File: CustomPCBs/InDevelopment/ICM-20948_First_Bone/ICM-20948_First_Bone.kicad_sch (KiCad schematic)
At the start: 14 parts, among them J1 Conn_01x04_MountingPin, T1 BSS138BKS_115, U1 ICM-20948, U2 HE6206-18NR

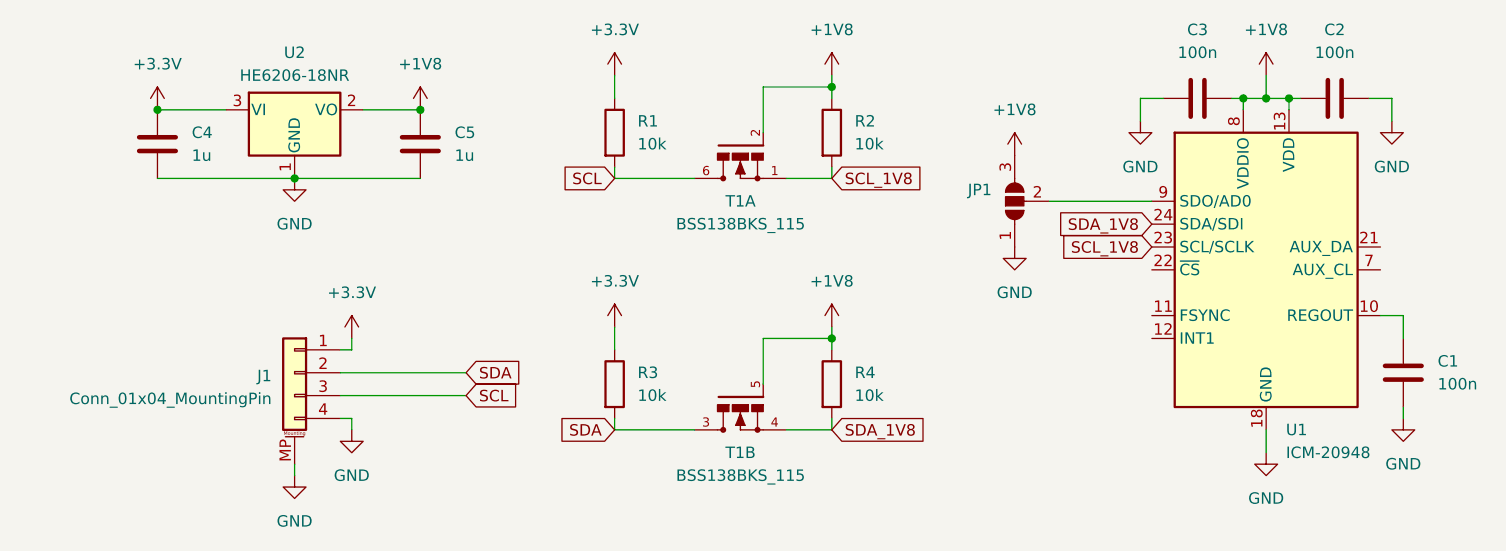
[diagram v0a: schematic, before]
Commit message: BMI160+mag board finished, fixed CS on ICM-20948
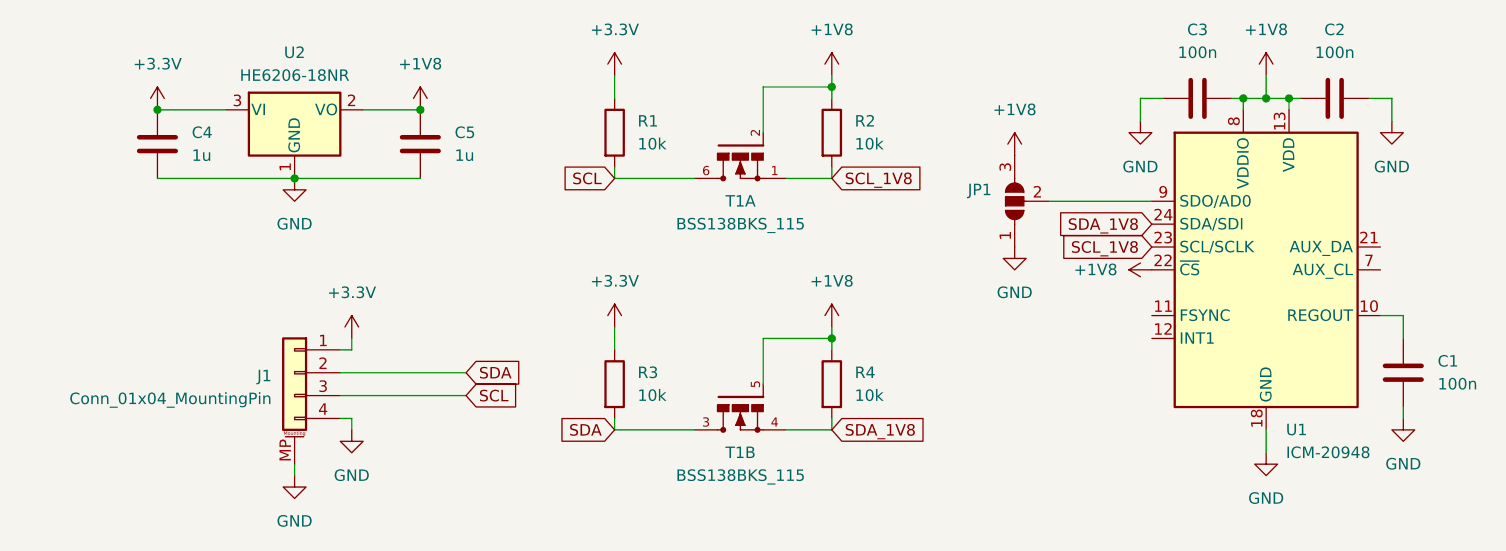
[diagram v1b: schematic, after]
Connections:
- net +1V8: now also U1.22 (~{CS})
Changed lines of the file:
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@@
+    )
+  )
+  (symbol (lib_id "power:+1V8") (at 207.01 57.15 90) (unit 1)
+    (in_bom yes) (on_board yes) (dnp no) (fields_autoplaced)
+    (property "Reference" "#PWR018" (at 210.82 57.15 0)
+      (effects (font (size 1.27 1.27)) hide)
+    )
+    (property "Value" "+1V8" (at 203.2 57.15 90)
+      (effects (font (size 1.27 1.27)) (justify left))
+    )
+    (property "Footprint" "" (at 207.01 57.15 0)
+      (effects (font (size 1.27 1.27)) hide)
+    )
+    (property "Datasheet" "" (at 207.01 57.15 0)
+      (effects (font (size 1.27 1.27)) hide)
+    )
+    (pin "1")
+    (instances
+      (project "ICM-20948_First_Bone"
+        (path "/f8f7ac55-fd20-42ea-9cac-b11904d84b21"
+          (reference "#PWR018") (unit 1)
+        )
+      )
     )
   )
